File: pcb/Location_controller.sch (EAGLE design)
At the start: 36 parts, among them IC1 LIS302DL, X1 22-23-2021

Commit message: Add connections to RCM
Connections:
- new net USART2_RX: JP2.19, U$1.PA3/ETH_MII_COL/ADC123_IN2(5T)
- new net USART2_TX: JP2.18, U$1.PA2/ETH_MDIO/ADC123_IN2(5T)
- net GND: now also JP2.15
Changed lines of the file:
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@@
 <part name="POWER" library="pinhead" deviceset="PINHD-1X3" device=""/>
 <part name="JP2" library="pinhead" deviceset="PINHD-1X20" device=""/>
+<part name="GND7" library="supply1" deviceset="GND" device=""/>
 </parts>
 <sheets>
@@
 <instance part="POWER" gate="A" x="-58.42" y="116.84" rot="R180"/>
 <instance part="JP2" gate="A" x="-50.8" y="-60.96" rot="R90"/>
+<instance part="GND7" gate="1" x="-38.1" y="-81.28"/>
 </instances>
 <busses>
@@
 <pinref part="GND6" gate="1" pin="GND"/>
 </segment>
+<segment>
+<pinref part="JP2" gate="A" pin="15"/>
+<wire x1="-38.1" y1="-63.5" x2="-38.1" y2="-78.74" width="0.1524" layer="91"/>
+<pinref part="GND7" gate="1" pin="GND"/>
+</segment>
 </net>
 <net name="N$1" class="0">
@@
 </segment>
 </net>
+<net name="USART2_TX" class="0">
+<segment>
+<pinref part="U$1" gate="G$1" pin="PA2/ETH_MDIO/ADC123_IN2(5T)"/>
+<wire x1="40.64" y1="66.04" x2="15.24" y2="66.04" width="0.1524" layer="91"/>
+<label x="15.24" y="66.04" size="1.778" layer="95"/>
+</segment>
+<segment>
+<pinref part="JP2" gate="A" pin="18"/>
+<wire x1="-30.48" y1="-63.5" x2="-30.48" y2="-78.74" width="0.1524" layer="91"/>
+<label x="-30.48" y="-83.82" size="1.778" layer="95" rot="R90"/>
+</segment>
+</net>
+<net name="USART2_RX" class="0">
+<segment>
+<pinref part="U$1" gate="G$1" pin="PA3/ETH_MII_COL/ADC123_IN2(5T)"/>
+<wire x1="40.64" y1="63.5" x2="15.24" y2="63.5" width="0.1524" layer="91"/>
+<label x="15.24" y="60.96" size="1.778" layer="95"/>
+</segment>
+<segment>
+<pinref part="JP2" gate="A" pin="19"/>
+<wire x1="-27.94" y1="-63.5" x2="-27.94" y2="-78.74" width="0.1524" layer="91"/>
+<label x="-25.4" y="-83.82" size="1.778" layer="95" rot="R90"/>
+</segment>
+</net>

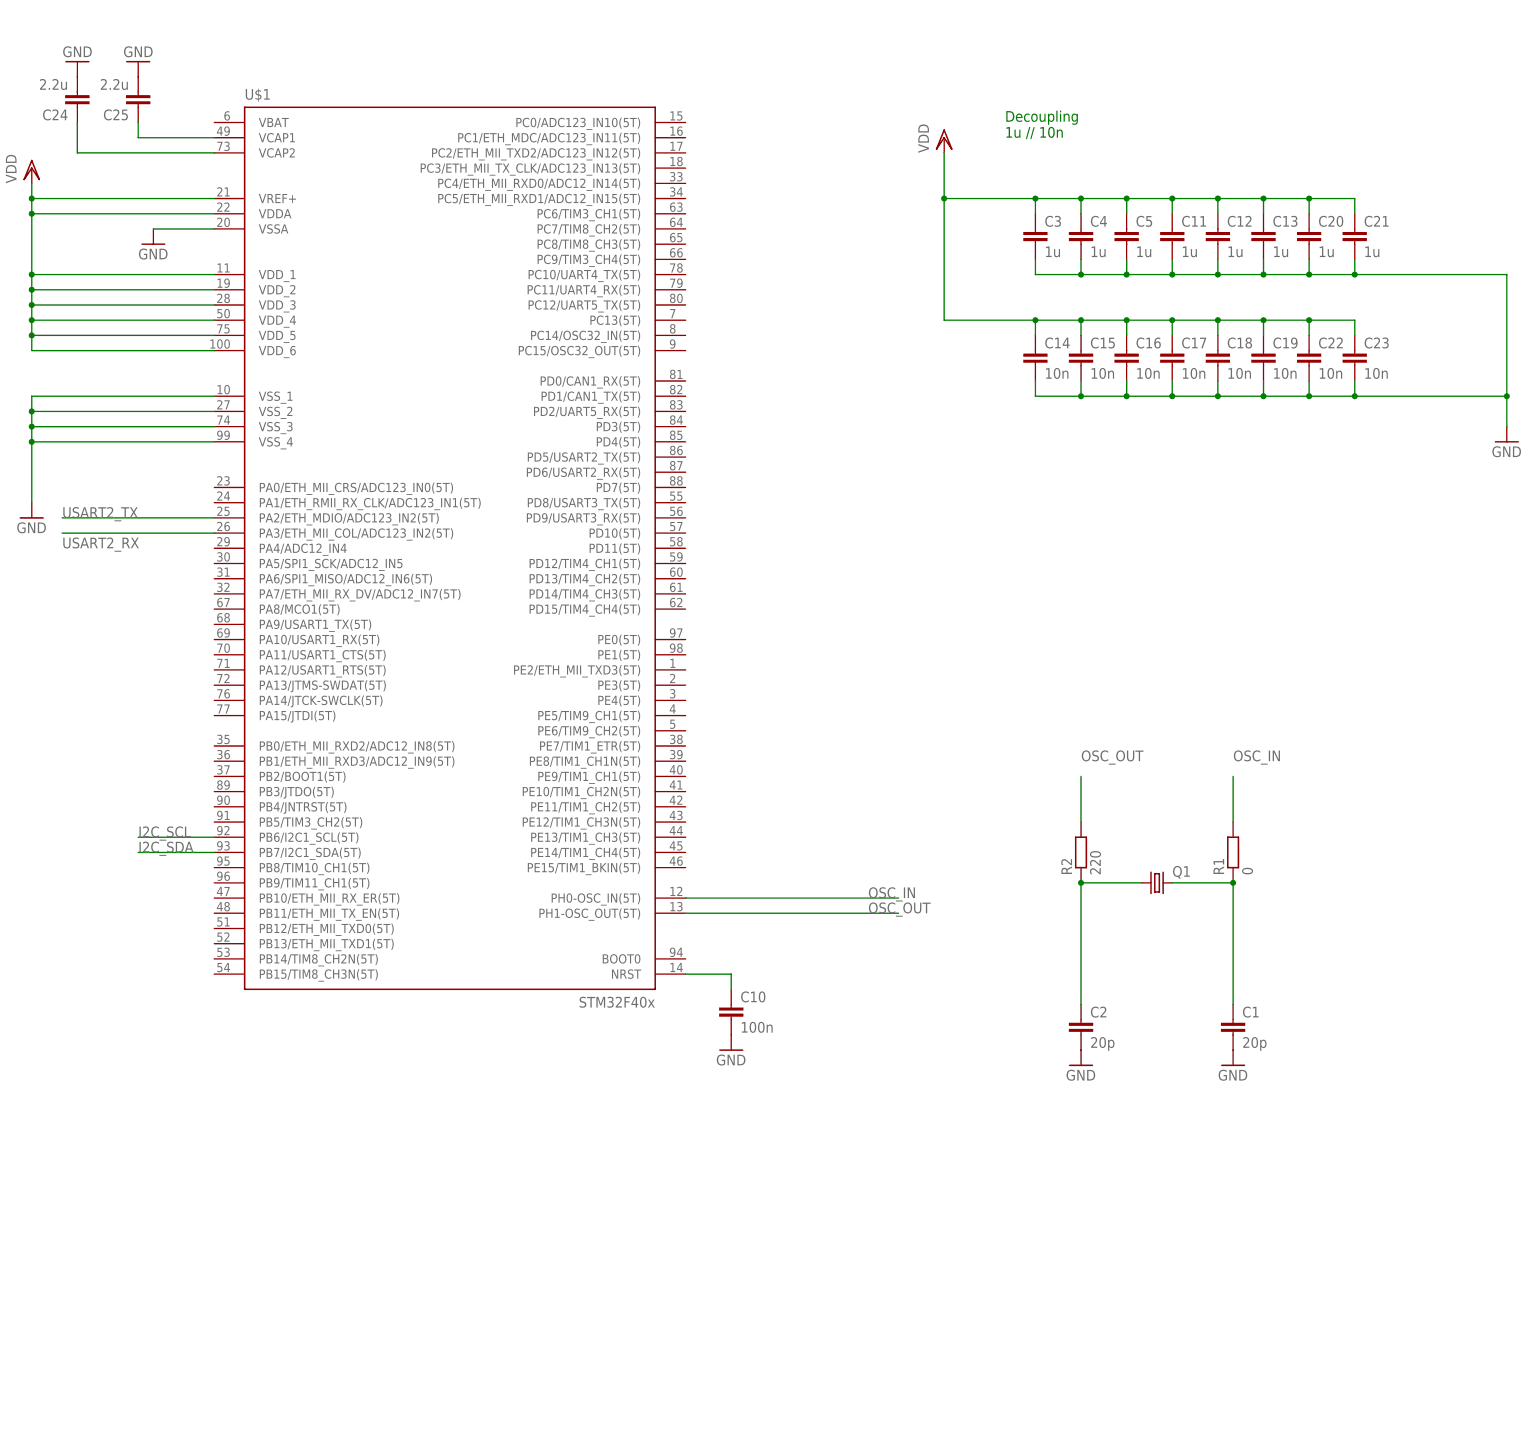
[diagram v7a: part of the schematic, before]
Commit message: Add SWD programmer connectors
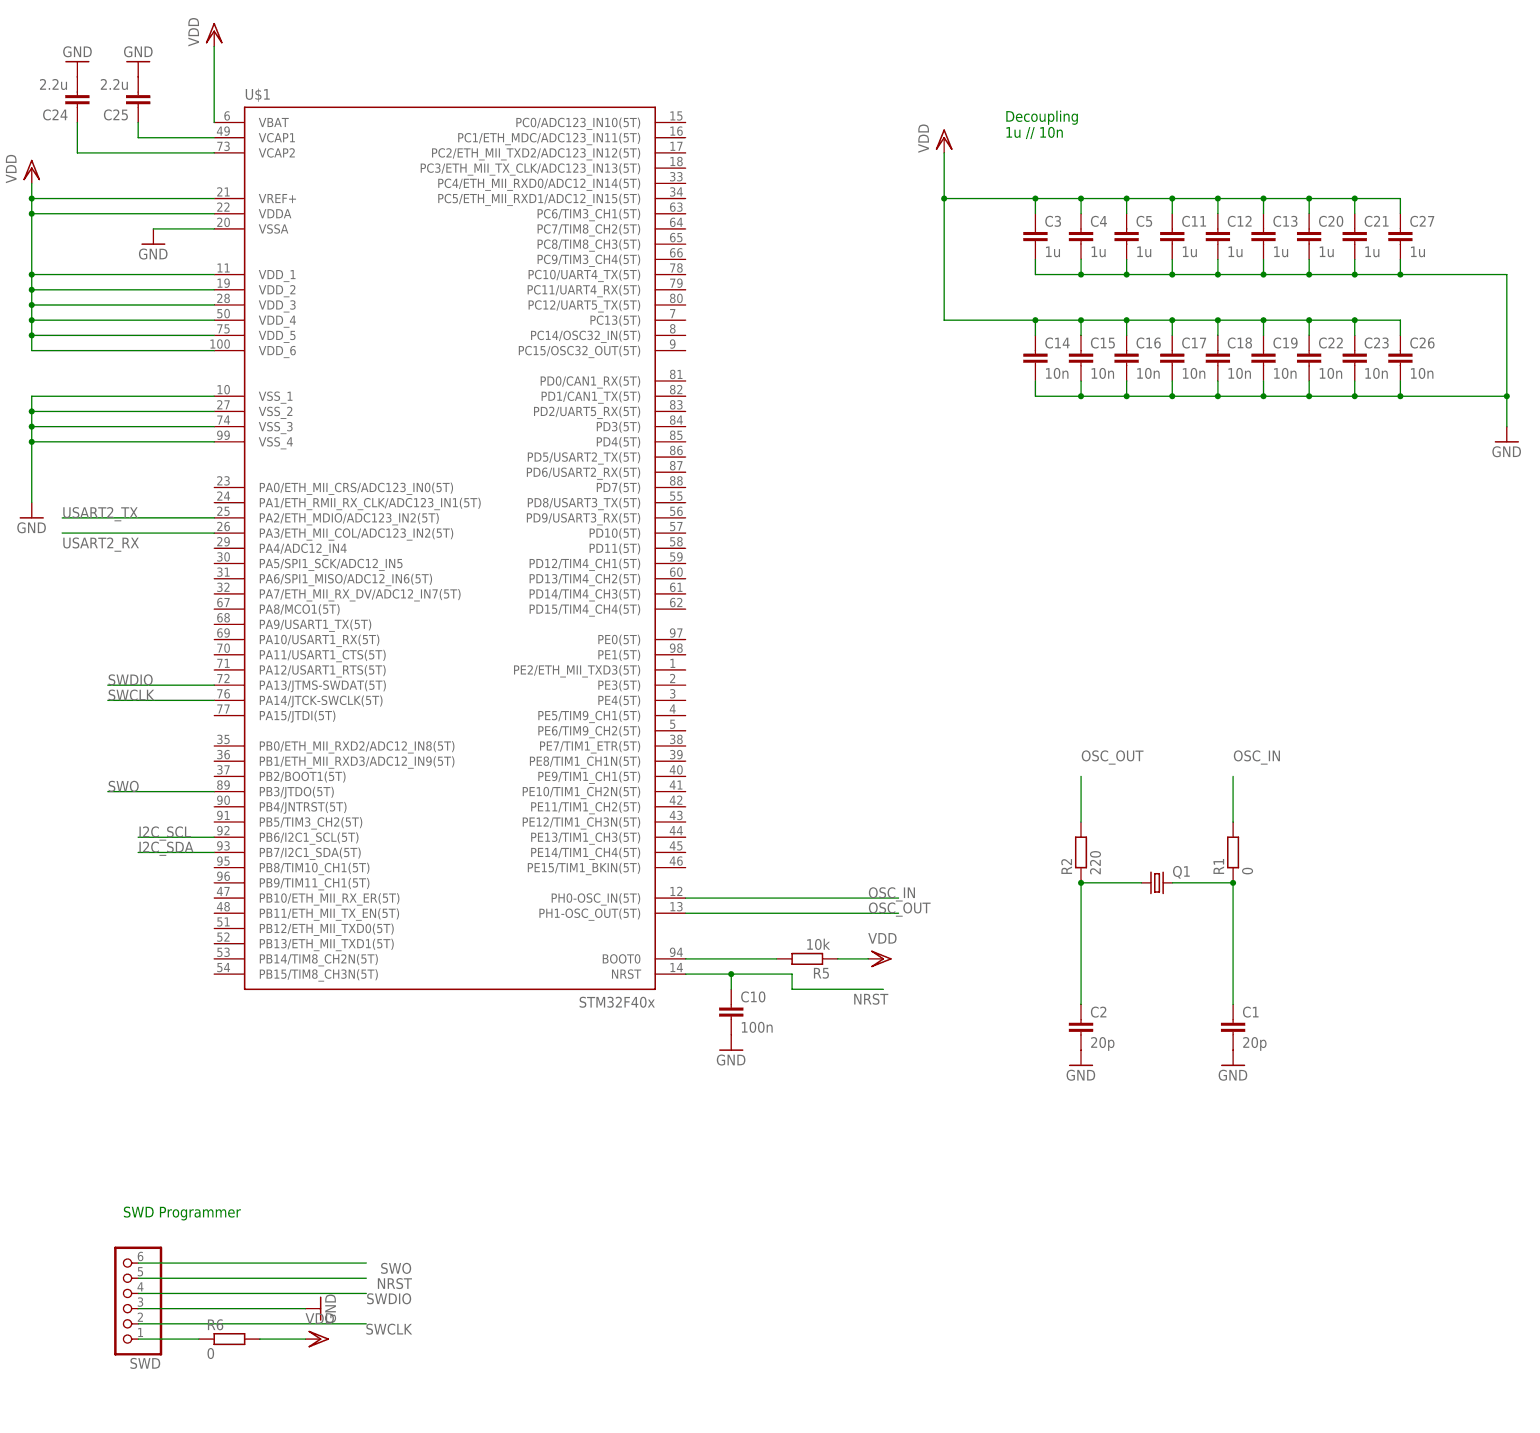
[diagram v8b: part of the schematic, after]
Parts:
- added C26: 10n, eagle-ltspice:C
- added C27: 1u, eagle-ltspice:C
- added R5: 10k, eagle-ltspice:R
- added R6: 0, eagle-ltspice:R
- added SWD: (no value), pinhead:PINHD-1X6
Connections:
- removed net N$5: C10.1, U$1.NRST
- new net N$3: R5.2, U$1.BOOT0
- new net N$6: R6.1, SWD.1
- new net NRST: C10.1, SWD.5, U$1.NRST
- new net SWCLK: SWD.2, U$1.PA14/JTCK-SWCLK(5T)
- new net SWDIO: SWD.4, U$1.PA13/JTMS-SWDAT(5T)
- new net SWO: SWD.6, U$1.PB3/JTDO(5T)
- net GND: now also C26.2, C27.2, SWD.3
- net VDD: now also C26.1, C27.1, R5.1, R6.2, U$1.VBAT
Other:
- note added: "SWD Programmer"
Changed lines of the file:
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@@
 <part name="JP2" library="pinhead" deviceset="PINHD-1X20" device=""/>
 <part name="GND7" library="supply1" deviceset="GND" device=""/>
+<part name="VDD2" library="supply1" deviceset="VDD" device=""/>
+<part name="R5" library="eagle-ltspice" deviceset="R" device="" value="10k"/>
+<part name="VDD8" library="supply1" deviceset="VDD" device=""/>
+<part name="C26" library="eagle-ltspice" deviceset="C" device="" value="10n"/>
+<part name="C27" library="eagle-ltspice" deviceset="C" device="" value="1u"/>
+<part name="SWD" library="pinhead" deviceset="PINHD-1X6" device=""/>
+<part name="R6" library="eagle-ltspice" deviceset="R" device="" value="0"/>
+<part name="VDD9" library="supply1" deviceset="VDD" device=""/>
+<part name="GND17" library="supply1" deviceset="GND" device=""/>
 </parts>
 <sheets>
@@
 <text x="-38.1" y="116.84" size="1.778" layer="91">Jumper selector</text>
 <text x="-76.2" y="-55.88" size="1.778" layer="91">Antenna Controller + Support</text>
+<text x="25.4" y="-50.8" size="1.778" layer="91">SWD Programmer</text>
 </plain>
 <instances>
@@
 <instance part="JP2" gate="A" x="-50.8" y="-60.96" rot="R90"/>
 <instance part="GND7" gate="1" x="-38.1" y="-81.28"/>
+<instance part="VDD2" gate="G$1" x="152.4" y="-7.62" rot="R270"/>
+<instance part="R5" gate="G$1" x="139.7" y="-7.62" rot="R180"/>
+<instance part="VDD8" gate="G$1" x="40.64" y="147.32"/>
+<instance part="C26" gate="G$1" x="238.76" y="93.98"/>
+<instance part="C27" gate="G$1" x="238.76" y="114.3"/>
+<instance part="SWD" gate="A" x="25.4" y="-63.5" rot="R180"/>
+<instance part="R6" gate="G$1" x="43.18" y="-71.12"/>
+<instance part="VDD9" gate="G$1" x="58.42" y="-71.12" rot="R270"/>
+<instance part="GND17" gate="1" x="58.42" y="-66.04" rot="R90"/>
 </instances>
 <busses>
@@
 <wire x1="215.9" y1="106.68" x2="223.52" y2="106.68" width="0.1524" layer="91"/>
 <wire x1="223.52" y1="106.68" x2="231.14" y2="106.68" width="0.1524" layer="91"/>
-<wire x1="231.14" y1="106.68" x2="256.54" y2="106.68" width="0.1524" layer="91"/>
+<wire x1="231.14" y1="106.68" x2="238.76" y2="106.68" width="0.1524" layer="91"/>
+<wire x1="238.76" y1="106.68" x2="256.54" y2="106.68" width="0.1524" layer="91"/>
 <wire x1="256.54" y1="106.68" x2="256.54" y2="86.36" width="0.1524" layer="91"/>
 <pinref part="C14" gate="G$1" pin="2"/>
@@
 <wire x1="215.9" y1="86.36" x2="223.52" y2="86.36" width="0.1524" layer="91"/>
 <wire x1="223.52" y1="86.36" x2="231.14" y2="86.36" width="0.1524" layer="91"/>
-<wire x1="231.14" y1="86.36" x2="256.54" y2="86.36" width="0.1524" layer="91"/>
+<wire x1="231.14" y1="86.36" x2="238.76" y2="86.36" width="0.1524" layer="91"/>
+<wire x1="238.76" y1="86.36" x2="256.54" y2="86.36" width="0.1524" layer="91"/>
 <wire x1="185.42" y1="88.9" x2="185.42" y2="86.36" width="0.1524" layer="91"/>
 <junction x="185.42" y="86.36"/>
@@
 <wire x1="231.14" y1="88.9" x2="231.14" y2="86.36" width="0.1524" layer="91"/>
 <junction x="231.14" y="86.36"/>
+<pinref part="C27" gate="G$1" pin="2"/>
+<wire x1="238.76" y1="109.22" x2="238.76" y2="106.68" width="0.1524" layer="91"/>
+<junction x="238.76" y="106.68"/>
+<pinref part="C26" gate="G$1" pin="2"/>
+<wire x1="238.76" y1="88.9" x2="238.76" y2="86.36" width="0.1524" layer="91"/>
+<junction x="238.76" y="86.36"/>
 </segment>
 <segment>
@@
 <wire x1="-38.1" y1="-63.5" x2="-38.1" y2="-78.74" width="0.1524" layer="91"/>
 <pinref part="GND7" gate="1" pin="GND"/>
+</segment>
+<segment>
+<pinref part="SWD" gate="A" pin="3"/>
+<pinref part="GND17" gate="1" pin="GND"/>
+<wire x1="27.94" y1="-66.04" x2="55.88" y2="-66.04" width="0.1524" layer="91"/>
 </segment>
 </net>
@@
 <wire x1="231.14" y1="99.06" x2="231.14" y2="96.52" width="0.1524" layer="91"/>
 <junction x="223.52" y="99.06"/>
+<pinref part="C27" gate="G$1" pin="1"/>
+<wire x1="238.76" y1="116.84" x2="238.76" y2="119.38" width="0.1524" layer="91"/>
+<wire x1="238.76" y1="119.38" x2="231.14" y2="119.38" width="0.1524" layer="91"/>
+<junction x="231.14" y="119.38"/>
+<pinref part="C26" gate="G$1" pin="1"/>
+<wire x1="238.76" y1="96.52" x2="238.76" y2="99.06" width="0.1524" layer="91"/>
+<wire x1="238.76" y1="99.06" x2="231.14" y2="99.06" width="0.1524" layer="91"/>
+<junction x="231.14" y="99.06"/>
 </segment>
 <segment>
@@
 <pinref part="POWER" gate="A" pin="2"/>
 <wire x1="-55.88" y1="116.84" x2="-43.18" y2="116.84" width="0.1524" layer="91"/>
+</segment>
+<segment>
+<pinref part="R5" gate="G$1" pin="1"/>
+<pinref part="VDD2" gate="G$1" pin="VDD"/>
+<wire x1="144.78" y1="-7.62" x2="149.86" y2="-7.62" width="0.1524" layer="91"/>
+</segment>
+<segment>
+<pinref part="U$1" gate="G$1" pin="VBAT"/>
+<pinref part="VDD8" gate="G$1" pin="VDD"/>
+<wire x1="40.64" y1="132.08" x2="40.64" y2="144.78" width="0.1524" layer="91"/>
+</segment>
+<segment>
+<pinref part="R6" gate="G$1" pin="2"/>
+<pinref part="VDD9" gate="G$1" pin="VDD"/>
+<wire x1="48.26" y1="-71.12" x2="55.88" y2="-71.12" width="0.1524" layer="91"/>
 </segment>
 </net>
@@
 </segment>
 </net>
-<net name="N$5" class="0">
-<segment>
-<pinref part="C10" gate="G$1" pin="1"/>
-<wire x1="127" y1="-12.7" x2="127" y2="-10.16" width="0.1524" layer="91"/>
-<pinref part="U$1" gate="G$1" pin="NRST"/>
-<wire x1="127" y1="-10.16" x2="119.38" y2="-10.16" width="0.1524" layer="91"/>
-</segment>
-</net>
 <net name="N$8" class="0">
 <segment>
@@
 </segment>
 </net>
+<net name="N$3" class="0">
+<segment>
+<pinref part="R5" gate="G$1" pin="2"/>
+<pinref part="U$1" gate="G$1" pin="BOOT0"/>
+<wire x1="134.62" y1="-7.62" x2="119.38" y2="-7.62" width="0.1524" layer="91"/>
+</segment>
+</net>
+<net name="N$6" class="0">
+<segment>
+<pinref part="SWD" gate="A" pin="1"/>
+<pinref part="R6" gate="G$1" pin="1"/>
+<wire x1="27.94" y1="-71.12" x2="38.1" y2="-71.12" width="0.1524" layer="91"/>
+</segment>
+</net>
+<net name="SWCLK" class="0">
+<segment>
+<pinref part="SWD" gate="A" pin="2"/>
+<wire x1="27.94" y1="-68.58" x2="66.04" y2="-68.58" width="0.1524" layer="91"/>
+<label x="73.66" y="-68.58" size="1.778" layer="95" rot="R180"/>
+</segment>
+<segment>
+<pinref part="U$1" gate="G$1" pin="PA14/JTCK-SWCLK(5T)"/>
+<wire x1="40.64" y1="35.56" x2="22.86" y2="35.56" width="0.1524" layer="91"/>
+<label x="22.86" y="35.56" size="1.778" layer="95"/>
+</segment>
+</net>
+<net name="SWO" class="0">
+<segment>
+<pinref part="SWD" gate="A" pin="6"/>
+<wire x1="27.94" y1="-58.42" x2="66.04" y2="-58.42" width="0.1524" layer="91"/>
+<label x="73.66" y="-58.42" size="1.778" layer="95" rot="R180"/>
+</segment>
+<segment>
+<pinref part="U$1" gate="G$1" pin="PB3/JTDO(5T)"/>
+<wire x1="40.64" y1="20.32" x2="22.86" y2="20.32" width="0.1524" layer="91"/>
+<label x="22.86" y="20.32" size="1.778" layer="95"/>
+</segment>
+</net>
+<net name="NRST" class="0">
+<segment>
+<pinref part="SWD" gate="A" pin="5"/>
+<wire x1="27.94" y1="-60.96" x2="66.04" y2="-60.96" width="0.1524" layer="91"/>
+<label x="73.66" y="-60.96" size="1.778" layer="95" rot="R180"/>
+</segment>
+<segment>
+<pinref part="C10" gate="G$1" pin="1"/>
+<wire x1="127" y1="-12.7" x2="127" y2="-10.16" width="0.1524" layer="91"/>
+<pinref part="U$1" gate="G$1" pin="NRST"/>
+<wire x1="127" y1="-10.16" x2="119.38" y2="-10.16" width="0.1524" layer="91"/>
+<wire x1="127" y1="-10.16" x2="137.16" y2="-10.16" width="0.1524" layer="91"/>
+<wire x1="137.16" y1="-10.16" x2="137.16" y2="-12.7" width="0.1524" layer="91"/>
+<junction x="127" y="-10.16"/>
+<wire x1="137.16" y1="-12.7" x2="152.4" y2="-12.7" width="0.1524" layer="91"/>
+<label x="147.32" y="-15.24" size="1.778" layer="95"/>
+</segment>
+</net>
+<net name="SWDIO" class="0">
+<segment>
+<pinref part="SWD" gate="A" pin="4"/>
+<wire x1="27.94" y1="-63.5" x2="66.04" y2="-63.5" width="0.1524" layer="91"/>
+<label x="73.66" y="-63.5" size="1.778" layer="95" rot="R180"/>
+</segment>
+<segment>
+<pinref part="U$1" gate="G$1" pin="PA13/JTMS-SWDAT(5T)"/>
+<wire x1="40.64" y1="38.1" x2="22.86" y2="38.1" width="0.1524" layer="91"/>
+<label x="22.86" y="38.1" size="1.778" layer="95"/>
+</segment>
+</net>
